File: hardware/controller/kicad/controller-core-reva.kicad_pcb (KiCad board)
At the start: 2 copper layers, 141.6 x 135.2 mm, 158 parts, among them J101 12V_ISOLATED_INPUT / JST XH, J102 STM_SWD / 1x6 2.54mm, J103 ESP_UART / 1x6 2.54mm, J104 UI_LINK / IDC 2x8 2.54mm, J105 JP13 NTC / 2 vías, J106 JP5 FLOW ADAPTER / VCC-GND-OC, J107 JP14 DOOR / contacto seco, J108 JP16 VISUAL V1..V8 / XH-8, J109 JP22 WATER / RED-WHITE-BLACK, J110 USB-C SERVICE / USB 2.0, J111 USB BENCH POWER / OPEN, J112 24V_ACTUATOR_INPUT / JST XH, J113 JP3 VALVE / JST XH, J114 POWER MONITOR / MEASURE ONLY, J115 JP8 GRINDER / 320VDC, J117 JP24 PUMP / 230VAC, J118 JP17 MAINS / L-N, J121 24V INTERNAL SELECT / OPEN FO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, K701 G5RL-1A-E-TV8 DC24, Q501 SI2308A, Q701 SI2308A / relay coil, U101 STM32G431RBT6, U201 ESP32-S3-WROOM-1U-N8R8, U203 USBLC6-2SC6, U301 AP63203WU-7, U302 TPS22918DBVR, U303 AP63200WU-7 / 24V to 12V, U501 DRV8876PWPR, U502 UCC27517DBVR, U601 TPS3828-33DBVR, U602 SN74LVC2G08DCTR, U603 SN74LVC2G08DCTR

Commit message: Swap JP16 motor outputs and document the manual routing plan
V1/V2 of JP16 now carry BREW_OUT2/BREW_OUT1 so both motor leads reach
J108 uncrossed once the DRV8876 moves beside it. Record the Freerouting
trial (kept as an experimental tool, not used by the build) and the
agreed next steps: move the H-bridge next to JP16, J102/J103 to the top
right, and route the remaining SELV blocks by hand.

Co-Authored-By: Claude Opus 5 <noreply@anthropic.com>
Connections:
- J108 pad 1: /BREW_OUT1 -> /BREW_OUT2
- J108 pad 2: /BREW_OUT2 -> /BREW_OUT1
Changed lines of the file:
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@@
 			(remove_unused_layers no)
 			(roundrect_rratio 0.147059)
-			(net "/BREW_OUT1")
+			(net "/BREW_OUT2")
 		)
 		(pad "2" thru_hole oval
@@
 			(layers "*.Cu" "*.Mask")
 			(remove_unused_layers no)
-			(net "/BREW_OUT2")
+			(net "/BREW_OUT1")
 		)
 		(pad "3" thru_hole oval

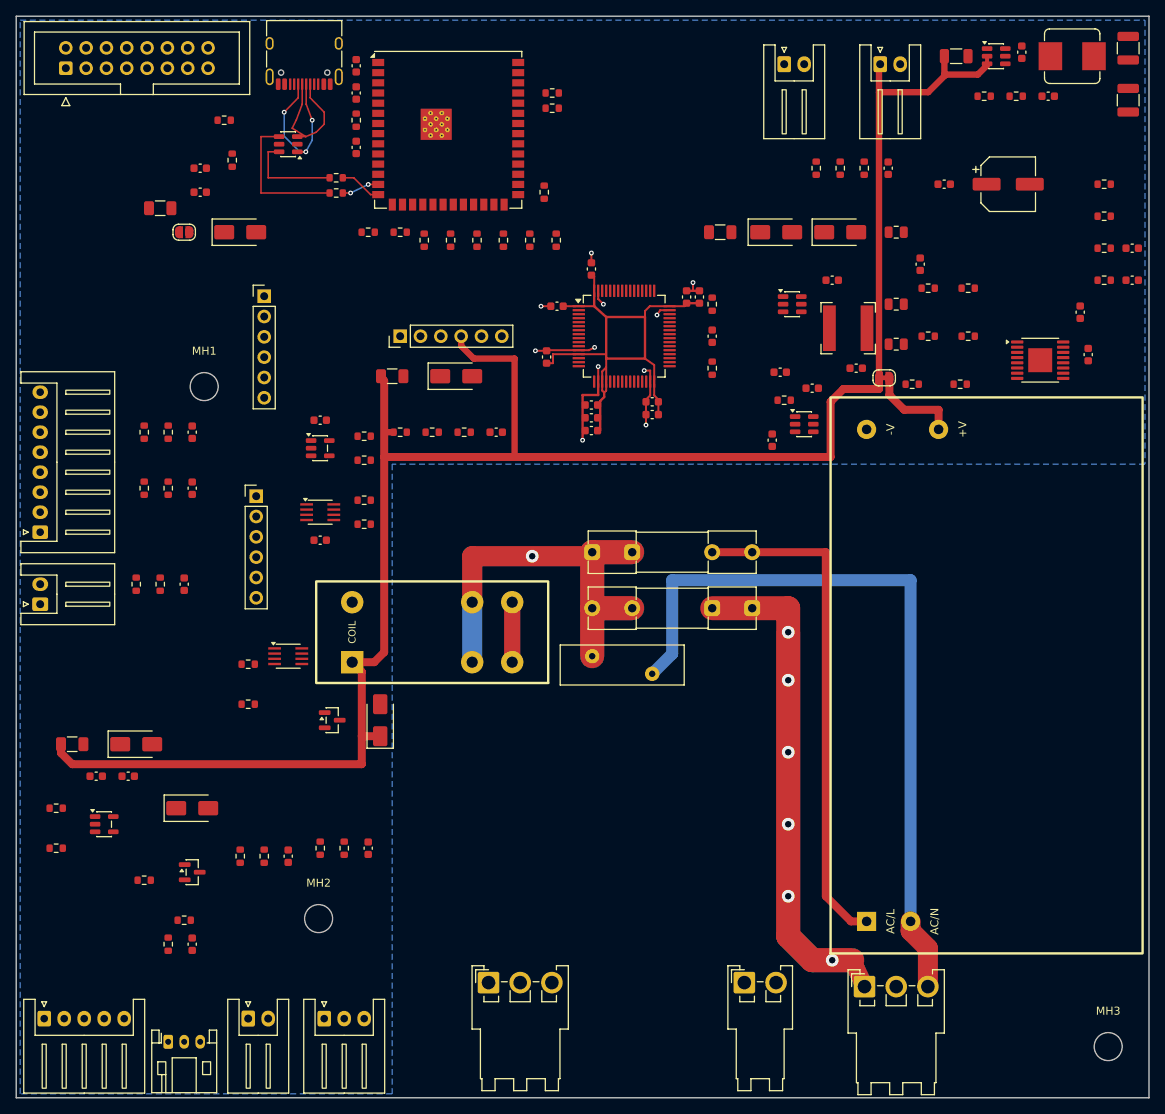
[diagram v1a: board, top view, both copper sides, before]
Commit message: Move the H-bridge beside JP16 and route it
Place U501 rotated 270 deg above MH1 with its charge pump, bulk and control
rows, F303/D304 inside the same block, and the debug headers in the freed
top-right corner. Route OUT1/OUT2 to J108, VM, the charge pump and the six
control rows; move the 24 V trunk to x = 46.4 mm and extend it to the relay
flyback diode and the relocated valve fuse. DRC: 0 violations apart from two
row ends still waiting for the STM32 signals; 236 connections remain.

Co-Authored-By: Claude Fable 5.1 <noreply@anthropic.com>
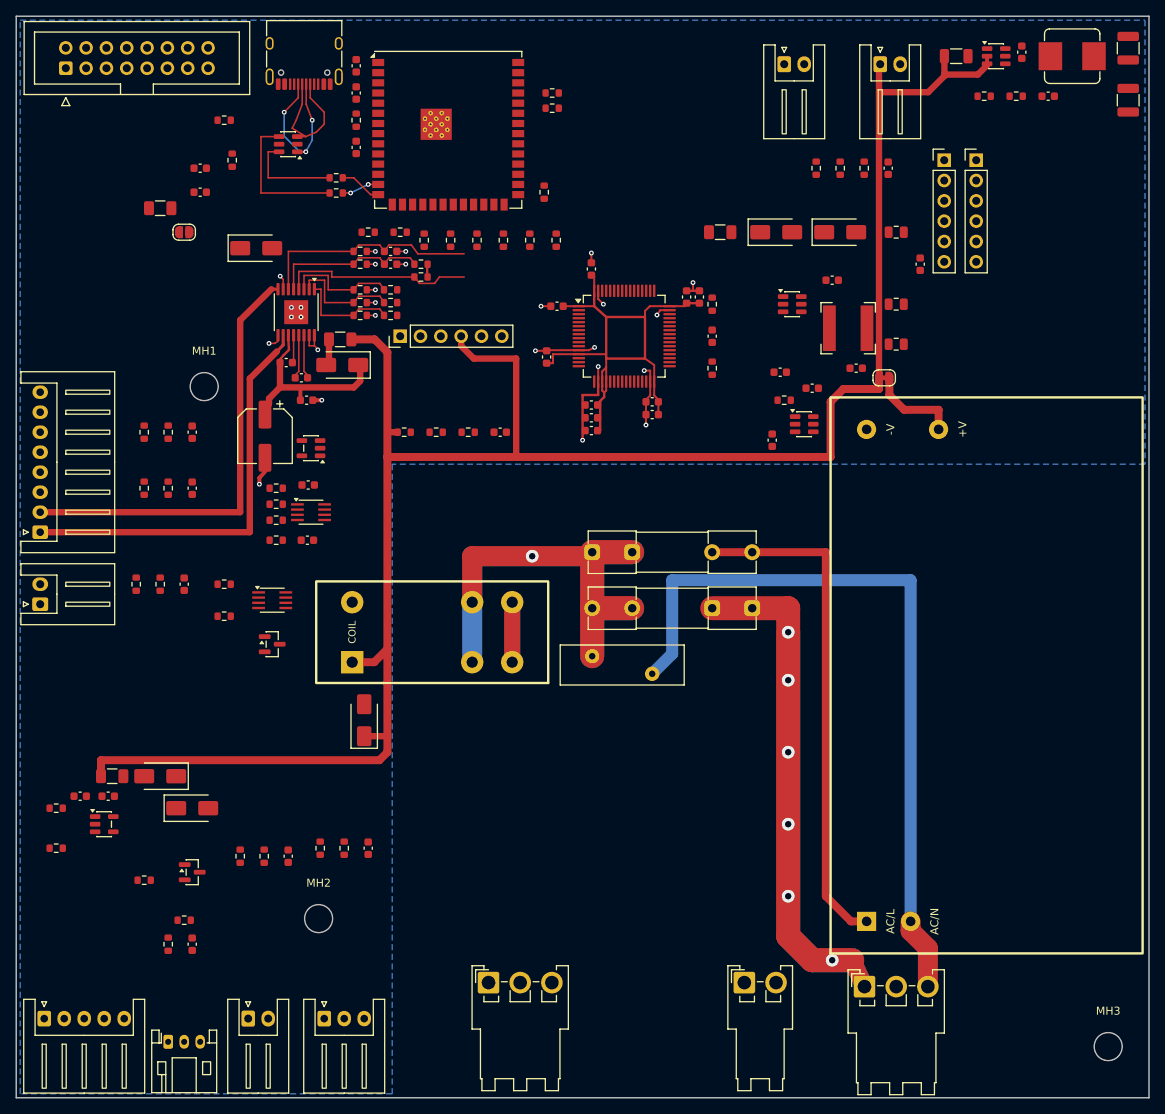
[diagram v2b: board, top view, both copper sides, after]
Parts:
- moved C503 99.4 mm to (33.8, 43.3), turned to 180 degrees
- moved C504 98.4 mm to (35.6, 45.2), turned to 0 degrees
- moved C501 98.1 mm to (31.1, 52.5), turned to -90 degrees
- moved J103 95.7 mm to (116.0, 18.0)
- moved U501 93.2 mm to (35.0, 37.0), turned to -90 degrees
- moved R510 93.1 mm to (43.0, 29.4)
- moved R509 93.0 mm to (43.0, 31.0)
- moved C506 92.8 mm to (46.8, 29.4)
- moved C505 92.7 mm to (46.8, 31.0)
- moved J102 90.6 mm to (120.0, 18.0)
- moved R507 86.2 mm to (50.6, 32.6), turned to 180 degrees
- moved R508 85.6 mm to (50.6, 31.0), turned to 180 degrees
- moved C502 84.1 mm to (36.3, 48.0)
- moved R504 76.1 mm to (43.0, 35.8)
- moved R502 76.1 mm to (43.0, 37.4)
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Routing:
- net /BREW_OUT1: track 0.00 -> 55.2 mm
- net /BREW_OUT2: track 0.00 -> 51.8 mm
- net /BREW_CURRENT_ADC: track 0.00 -> 27.7 mm
- net /BREW_FAULT_N: track 0.00 -> 23.6 mm
- net /24V_BREW: track 0.00 -> 21.3 mm
- net /BREW_VREF: track 0.00 -> 19.1 mm
- net /GND_UI: track 32.7 -> 47.8 mm, vias 11 -> 27
- net /BREW_SLEEP_DRV: track 0.00 -> 13.6 mm
- net /BREW_DIR_DRV: track 0.00 -> 13.4 mm
- net /BREW_EN_DRV: track 0.00 -> 12.8 mm
- net /24V_ACT_RAW: track 244.5 -> 251.3 mm
- net /BREW_CPH: track 0.00 -> 4.74 mm
- net /BREW_CPL: track 0.00 -> 4.74 mm
- net /BREW_VCP: track 0.00 -> 2.65 mm
- net /24V_BREW_FUSED: track 0.00 -> 2.00 mm
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
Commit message: Route the supervisor, interlocks and relay coil driver
Tuck R601/R602 under U601 and flip U603 so its outputs face the gate
resistors, keeping the 1.35 mm channel west of U601/U602 empty for STM_NRST.
Route the 3V3 spine through U601, C601, U602 and C602, the watchdog kick
chain, the valve arm pull-down, every ground pin on its own via, and the
relay chain from U603 through R801/R802 and Q701 to the K701 coil and D701.
Move the SWD and UART headers next to their chips: J102 above the STM32 and
J103 beside the ESP32. DRC clean; 212 connections remain.

Co-Authored-By: Claude Opus 5 <noreply@anthropic.com>
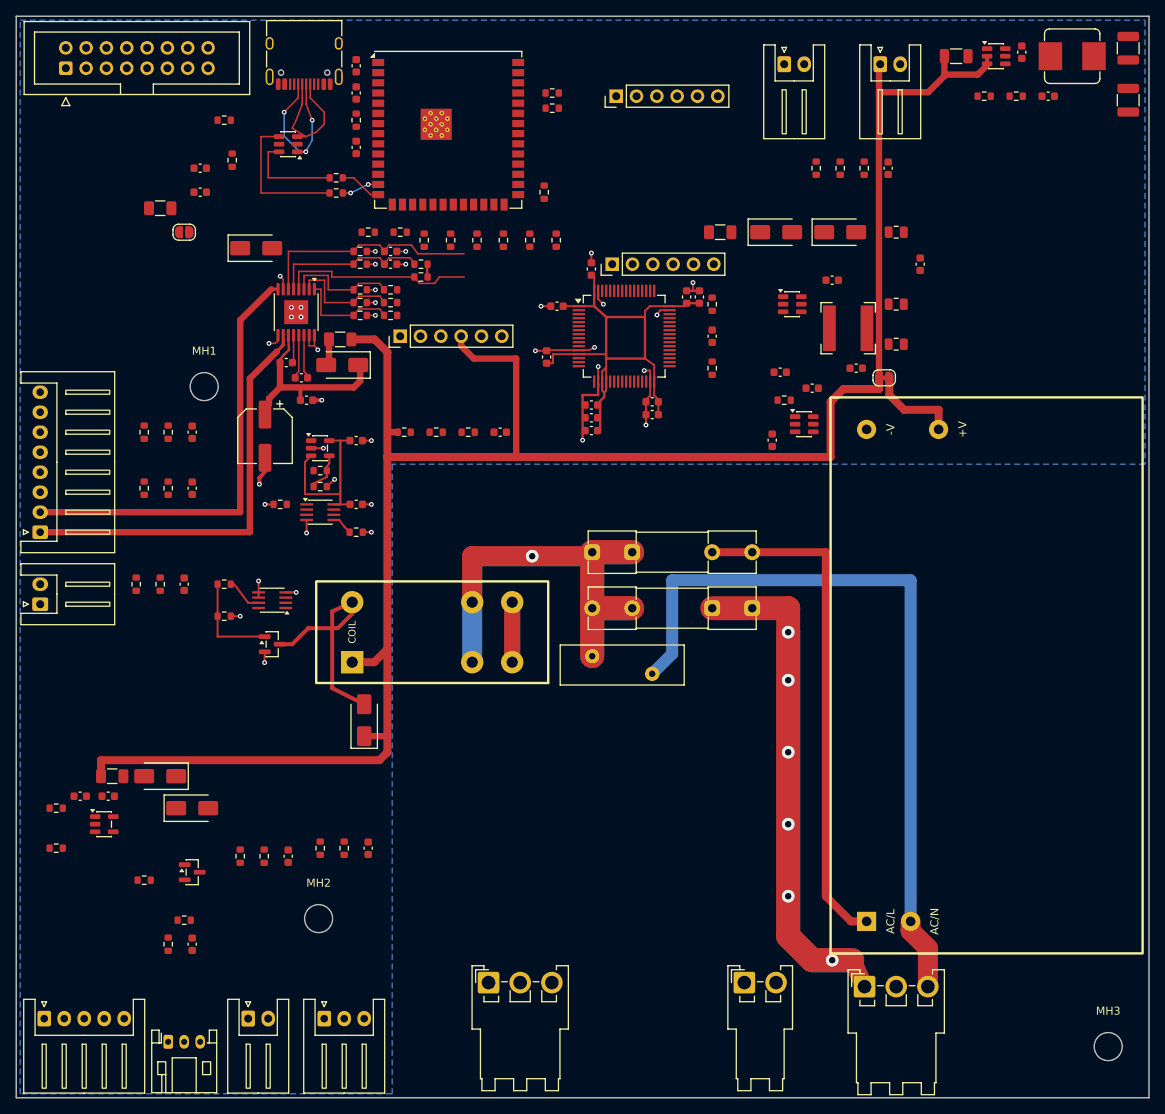
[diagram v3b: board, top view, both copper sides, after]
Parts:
- moved J102 47.3 mm to (74.5, 31.0), turned to 90 degrees
- moved J103 41.8 mm to (75.0, 10.0), turned to 90 degrees
- moved R604 10.0 mm to (42.5, 64.5), turned to 0 degrees
- moved C601 8.17 mm to (42.5, 53.0)
- moved C602 7.57 mm to (42.5, 61.0), turned to 0 degrees
- moved R601 5.92 mm to (38.0, 56.8)
- moved R602 5.92 mm to (38.0, 58.8)
- moved R603 2.04 mm to (33.0, 61.0)
- moved U601 1.15 mm to (38.0, 54.0), turned to 0 degrees
- moved U602 1.15 mm to (38.0, 62.0)
- turned U603 to 180 degrees
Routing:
- net /MAINS_RELAY_RETURN: track 0.00 -> 28.9 mm
- net /3V3_CORE: track 62.8 -> 83.8 mm
- net /GND_UI: track 47.8 -> 62.6 mm, vias 27 -> 38
- net /MAINS_RELAY_GATE: track 0.00 -> 12.4 mm
- net /WATCHDOG_KICK: track 0.00 -> 4.99 mm
- net /MAINS_RELAY_EN: track 0.00 -> 4.21 mm
- net /VALVE_EN_RAW: track 0.00 -> 1.99 mm

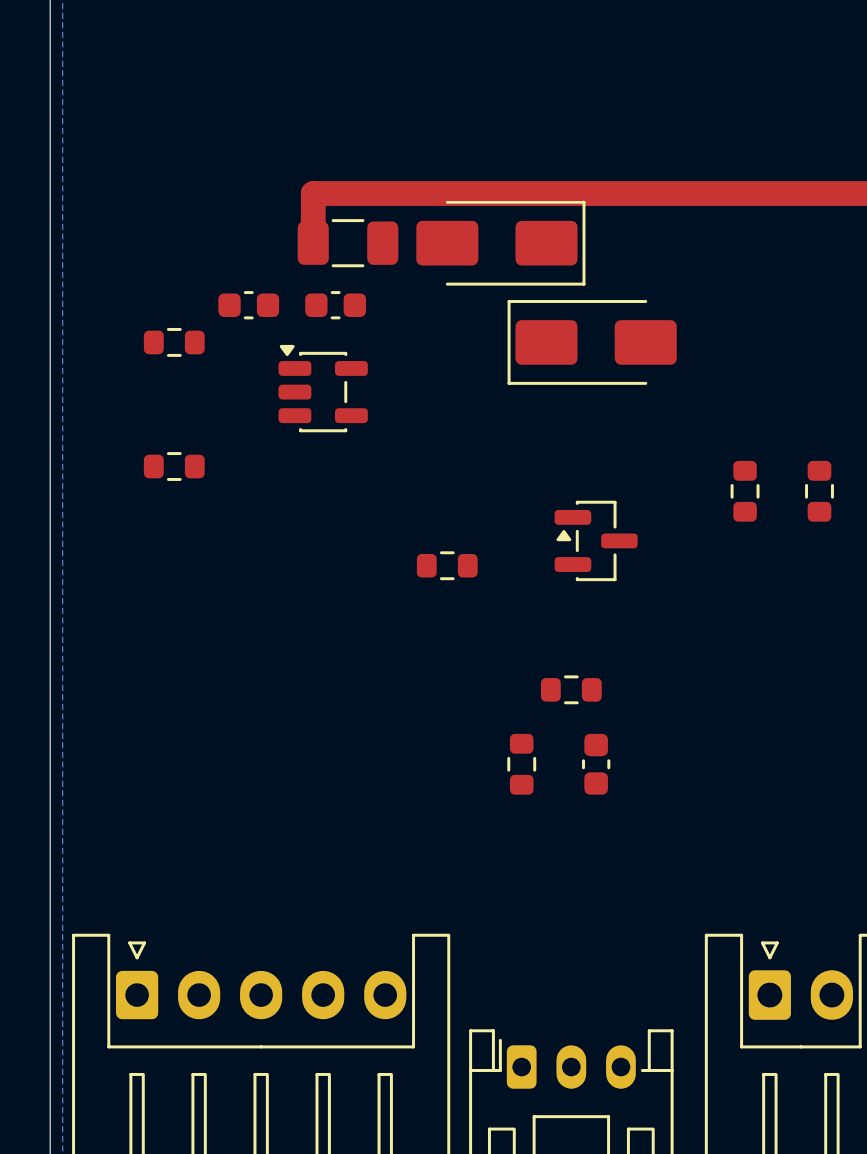
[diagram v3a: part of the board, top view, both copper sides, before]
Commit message: Route the valve branch
Route F304 to D305, the flyback diode, the 12 V driver supply, the enable and
gate chains, and the 24 V pair down the left edge to JP3. The 24 V branch dips
to B.Cu for 2.6 mm to pass under the 24 V trunk at y = 93 mm instead of
detouring around the sensor block. DRC clean; 193 connections remain.

Co-Authored-By: Claude Opus 5 <noreply@anthropic.com>
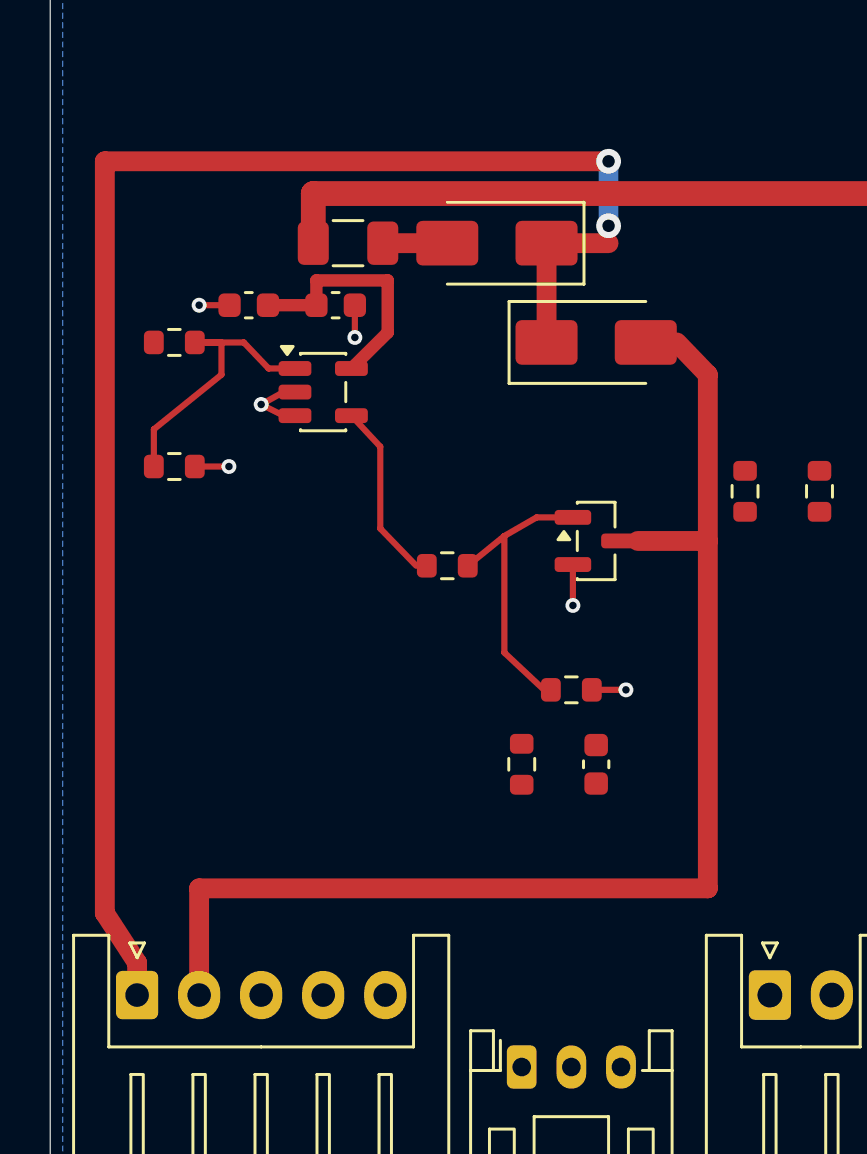
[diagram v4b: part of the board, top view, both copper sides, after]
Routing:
- net /24V_VALVE: track 0.00 -> 63.4 mm, vias 0 -> 2
- net /VALVE_RETURN: track 0.00 -> 50.1 mm
- net /VALVE_GATE: track 0.00 -> 11.2 mm
- net /VALVE_EN_DRV: track 0.00 -> 11.0 mm
- net /12V_PROTECTED: track 0.00 -> 9.58 mm
- net /GND_UI: track 62.6 -> 71.6 mm, vias 38 -> 44
- net /VALVE_GATE_RAW: track 0.00 -> 7.09 mm
- net /24V_VALVE_FUSED: track 0.00 -> 2.60 mm

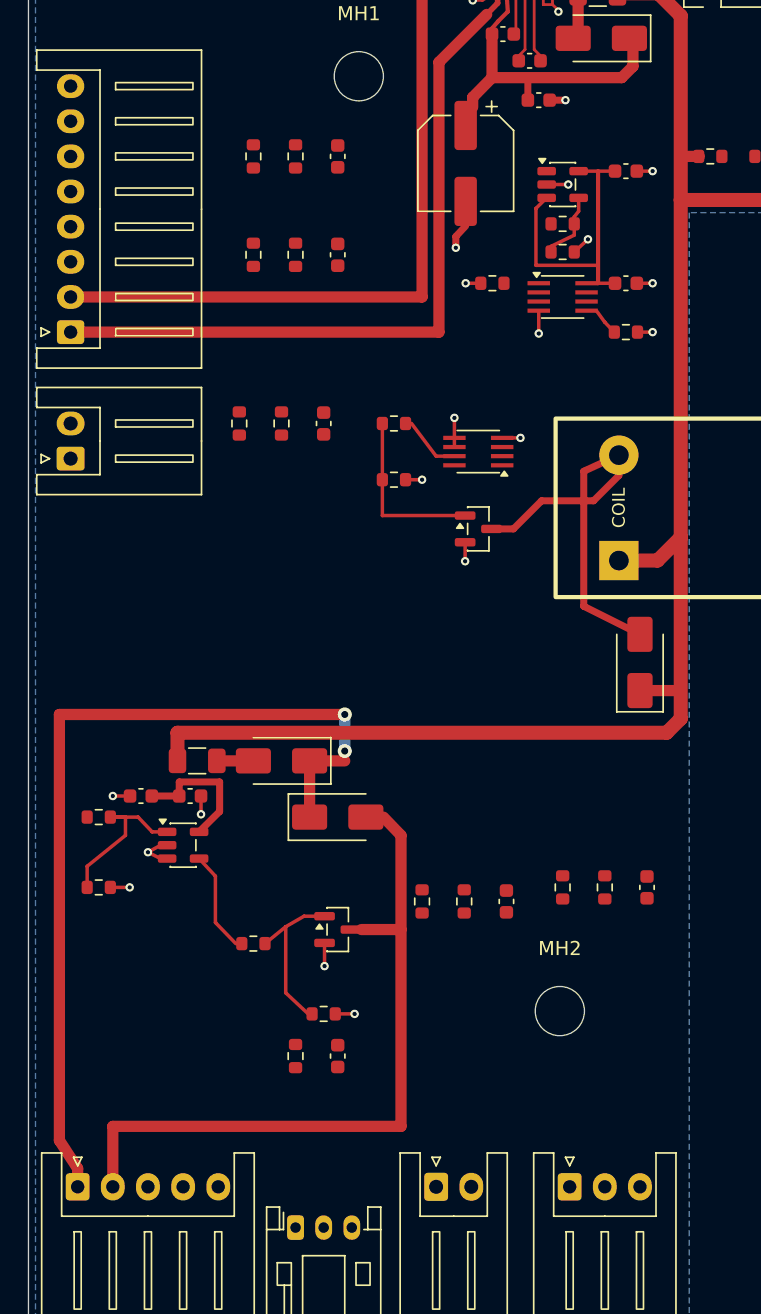
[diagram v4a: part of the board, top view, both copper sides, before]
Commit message: Route the sensor harness side
Route the NTC, flow, water level, door and both brew-unit contacts from their
connectors into their pull-up, series and filter rows, with the JP16 contact
common strapped and every filter capacitor grounded on its own via. The
working contact climbs east of MH1 and C501 so it never crosses the present
row. DRC clean; 169 connections remain.

Co-Authored-By: Claude Opus 5 <noreply@anthropic.com>
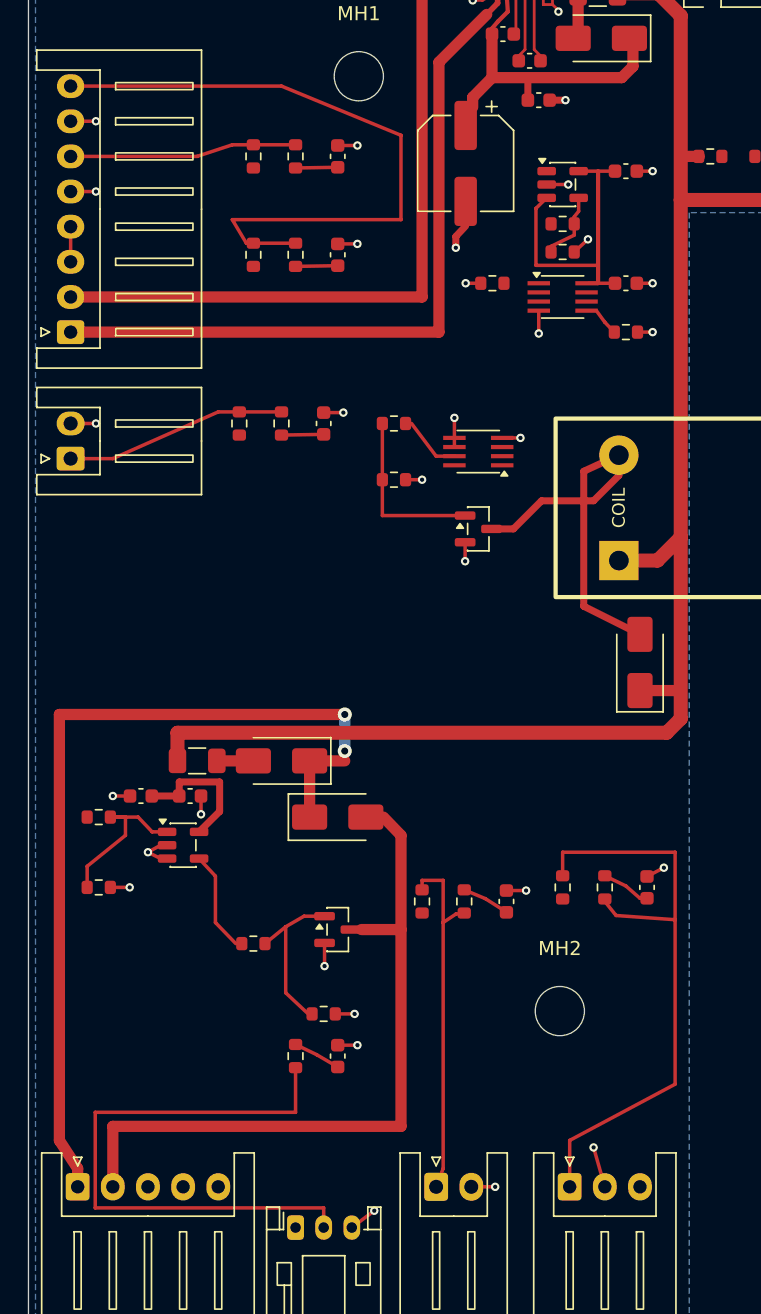
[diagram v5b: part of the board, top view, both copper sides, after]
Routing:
- net /BU_WORK_RAW: track 0.00 -> 47.6 mm
- net /FLOW_RAW: track 0.00 -> 43.2 mm
- net /WATER_RAW: track 0.00 -> 41.7 mm
- net /NTC_RAW: track 0.00 -> 25.5 mm
- net /GND_UI: track 71.6 -> 91.9 mm, vias 44 -> 56
- net /BU_PRESENT_RAW: track 0.00 -> 16.1 mm
- net /DOOR_RAW: track 0.00 -> 15.7 mm
- net /FLOW_TIM: track 0.00 -> 3.49 mm
- net /WATER_LEVEL: track 0.00 -> 3.40 mm
- net /DOOR_CLOSED_N: track 0.00 -> 3.00 mm
- net /BU_WORK_N: track 0.00 -> 3.00 mm
- net /BU_PRESENT_N: track 0.00 -> 3.00 mm
- net /NTC_ADC: track 0.00 -> 2.93 mm
- net /BU_BRIDGE: track 0.00 -> 2.50 mm
